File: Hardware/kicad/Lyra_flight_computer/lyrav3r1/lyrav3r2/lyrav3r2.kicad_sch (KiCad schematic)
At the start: 106 parts, among them IC1 TESEO-LIV3F, J1 Conn_01x02, J2 Screw_Terminal_01x04, J4 Conn_01x02, J5 Conn_01x05, J6 Screw_Terminal_01x05, J7 USB_B_Micro, Q1 AO3401A, Q2 AO3400A, Q4 AO3400A, Q5 AO3400A, Q9 AO3400A, U1 E22-900MM22S, U2 BMI088, U3 BMP388, U4 LIS3MDLTR, U5 ADXL375BCCZ-RL7, U6 RT9013-33GB_C19268157, U7 WS7916S-6/TR, U8 RP2040, U9 W25Q128JVS, X2 SX1M12.000M10F30TNN

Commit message: asd
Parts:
- removed FL1: SAFEA1G58KA0F00R15, .pretty:FILTER-SMD_5P-L1.4-W1.1-L, symbol .kicad_sym:SAFEA1G58KA0F00R15
- added C31, C35: 56p, Capacitor_SMD:C_0603_1608Metric, symbol Device:C_Small
- L1: value 10n -> 27n; LCSC Part C27147 -> (none)
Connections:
- net GND: now also C31.2, C35.2
- net GPSRX: now also C31.1
- net GPSTX: now also C35.1
- net at U7.6 (RFOUT): now also C33.1
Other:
- note removed: "Hardware guide says 27nh, but jlc only has 10nh but it should be fine?"
- moved on the sheet: C33

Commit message: work, inital layout
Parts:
- removed C15: 120p, Capacitor_SMD:C_0402_1005Metric, symbol Device:C_Small
- removed U7: WS7916S-6/TR, .pretty:DFN-6_L1.5-W1.0-P0.50-BL, symbol .kicad_sym:WS7916S-6_TR
- added FL1: SAFEA1G58KA0F00R15, .pretty:FILTER-SMD_5P-L1.4-W1.1-L, symbol .kicad_sym:SAFEA1G58KA0F00R15
- added U10: MXDLN16TL, .pretty:LGA-6_L1.1-W0.7-P0.40-BL, symbol .kicad_sym:MXDLN16TL
- BZ1: footprint SamacSys_Parts:CPT1414680T -> Connector_PinHeader_1.27mm:PinHeader_1x02_P1.27mm_Vertical
- JP1: footprint (none) -> Jumper:SolderJumper-3_P1.3mm_Open_RoundedPad1.0x1.5mm
- L1: LCSC Part (none) -> C381884
- L4: value 5n6 -> 14n; footprint Inductor_SMD:L_0402_1005Metric -> Inductor_SMD:L_0603_1608Metric; LCSC Part C27147 -> C346297
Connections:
- net ANT IN: now also L4.1
- net ANT OFF: now also U10.6 (EN)
- net BATT POSTSW: now also J2.4 (Pin_4); no longer J2.3 (Pin_3)
- net BATT RAW: now also J2.3 (Pin_3); no longer J2.4 (Pin_4)
- net GND: now also FL1.2 (GND), FL1.3 (GND), FL1.5 (GND), U10.1 (GND), U10.4 (GND)
- net VCC RF: now also U10.2 (VDD)
- net at L4.2: now also U10.5 (RFIN)
- net at C33.1: now also FL1.4 (OUT)
- new net: FL1.1 (IN), U10.3 (RFOUT)
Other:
- note added: "LNA"
- note removed: "LNA and SAW filter"
- moved on the sheet: C14, C16, C17, C18, C19, C21, C22, C23, C24, C25, C26, C27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

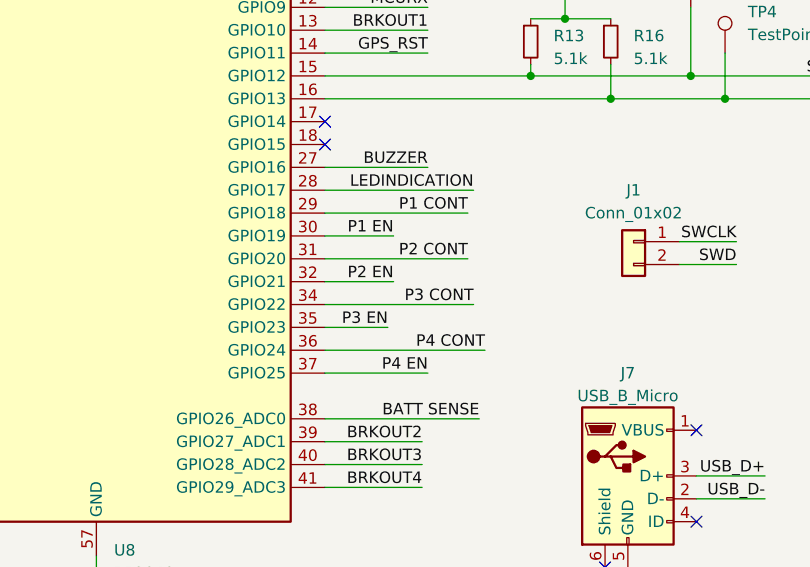
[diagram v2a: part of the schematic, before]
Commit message: first pass at routing
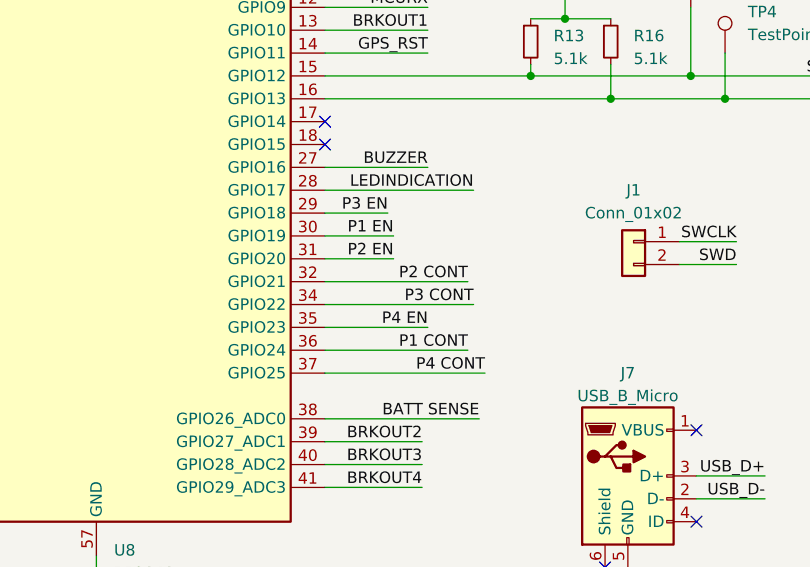
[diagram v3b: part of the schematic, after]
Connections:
- net P1 CONT : now also U8.36 (GPIO24); no longer U8.29 (GPIO18)
- net P2 CONT : now also U8.32 (GPIO21); no longer U8.31 (GPIO20)
- net P2 EN : now also U8.31 (GPIO20); no longer U8.32 (GPIO21)
- net P3 EN : now also U8.29 (GPIO18); no longer U8.35 (GPIO23)
- net P4 CONT : now also U8.37 (GPIO25); no longer U8.36 (GPIO24)
- net P4 EN : now also U8.35 (GPIO23); no longer U8.37 (GPIO25)
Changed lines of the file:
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@@
 	(wire
 		(pts
-			(xy 182.245 368.3) (xy 175.26 368.3)
+			(xy 182.245 355.6) (xy 175.26 355.6)
 		)
 		(stroke
@@
 	(wire
 		(pts
-			(xy 191.135 360.68) (xy 175.26 360.68)
+			(xy 191.135 363.22) (xy 175.26 363.22)
 		)
 		(stroke
@@
 	(wire
 		(pts
-			(xy 191.135 355.6) (xy 175.26 355.6)
+			(xy 191.135 370.84) (xy 175.26 370.84)
 		)
 		(stroke
@@
 	(wire
 		(pts
-			(xy 182.88 363.22) (xy 175.26 363.22)
+			(xy 182.88 360.68) (xy 175.26 360.68)
 		)
 		(stroke
@@
 	(wire
 		(pts
-			(xy 175.26 373.38) (xy 186.69 373.38)
+			(xy 175.26 368.3) (xy 186.69 368.3)
 		)
 		(stroke
@@
 	(wire
 		(pts
-			(xy 193.04 370.84) (xy 175.26 370.84)
+			(xy 193.04 373.38) (xy 175.26 373.38)
 		)
 		(stroke
@@
 	)
 	(label "P2 CONT "
-		(at 191.135 360.68 180)
+		(at 191.135 363.22 180)
 		(fields_autoplaced yes)
 		(effects
@@
 	)
 	(label "P1 CONT "
-		(at 191.135 355.6 180)
+		(at 191.135 370.84 180)
 		(fields_autoplaced yes)
 		(effects
@@
 	)
 	(label "P4 CONT "
-		(at 193.04 370.84 180)
+		(at 193.04 373.38 180)
 		(fields_autoplaced yes)
 		(effects
@@
 	)
 	(label "P2 EN "
-		(at 182.88 363.22 180)
+		(at 182.88 360.68 180)
 		(fields_autoplaced yes)
 		(effects
@@
 	)
 	(label "P4 EN "
-		(at 186.69 373.38 180)
+		(at 186.69 368.3 180)
 		(fields_autoplaced yes)
 		(effects
@@
 	)
 	(label "P3 EN "
-		(at 182.245 368.3 180)
+		(at 182.245 355.6 180)
 		(fields_autoplaced yes)
 		(effects

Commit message: EOD 6/24
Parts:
- added D1: D_Schottky, Diode_SMD:D_SOD-323F, symbol Device:D_Schottky
- added Q3: AO3401A, Package_TO_SOT_SMD:SOT-23, symbol Transistor_FET:AO3401A
- BZ1: Part # 490-CPT-14146-80T -> CPE-163
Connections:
- net +BATT: now also Q3.2 (S); no longer Q1.2 (S)
- net GND: now also Q3.1 (G); no longer Q1.1 (G)
- net VBUS: now reaches J7.1 (VBUS)
- net VBUS: now also Q1.1 (G), D1.2 (A)
- new net: D1.1 (K), Q1.2 (S), Q3.3 (D)
- no-connect marks 30 -> 29
